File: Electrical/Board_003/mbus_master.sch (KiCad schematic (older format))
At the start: 14 parts, among them J1 Conn_01x02, J2 Conn_01x02, J3 Conn_01x02, Q1 BC337, Q2 BC337, Q3 BC337, Q4 BD136

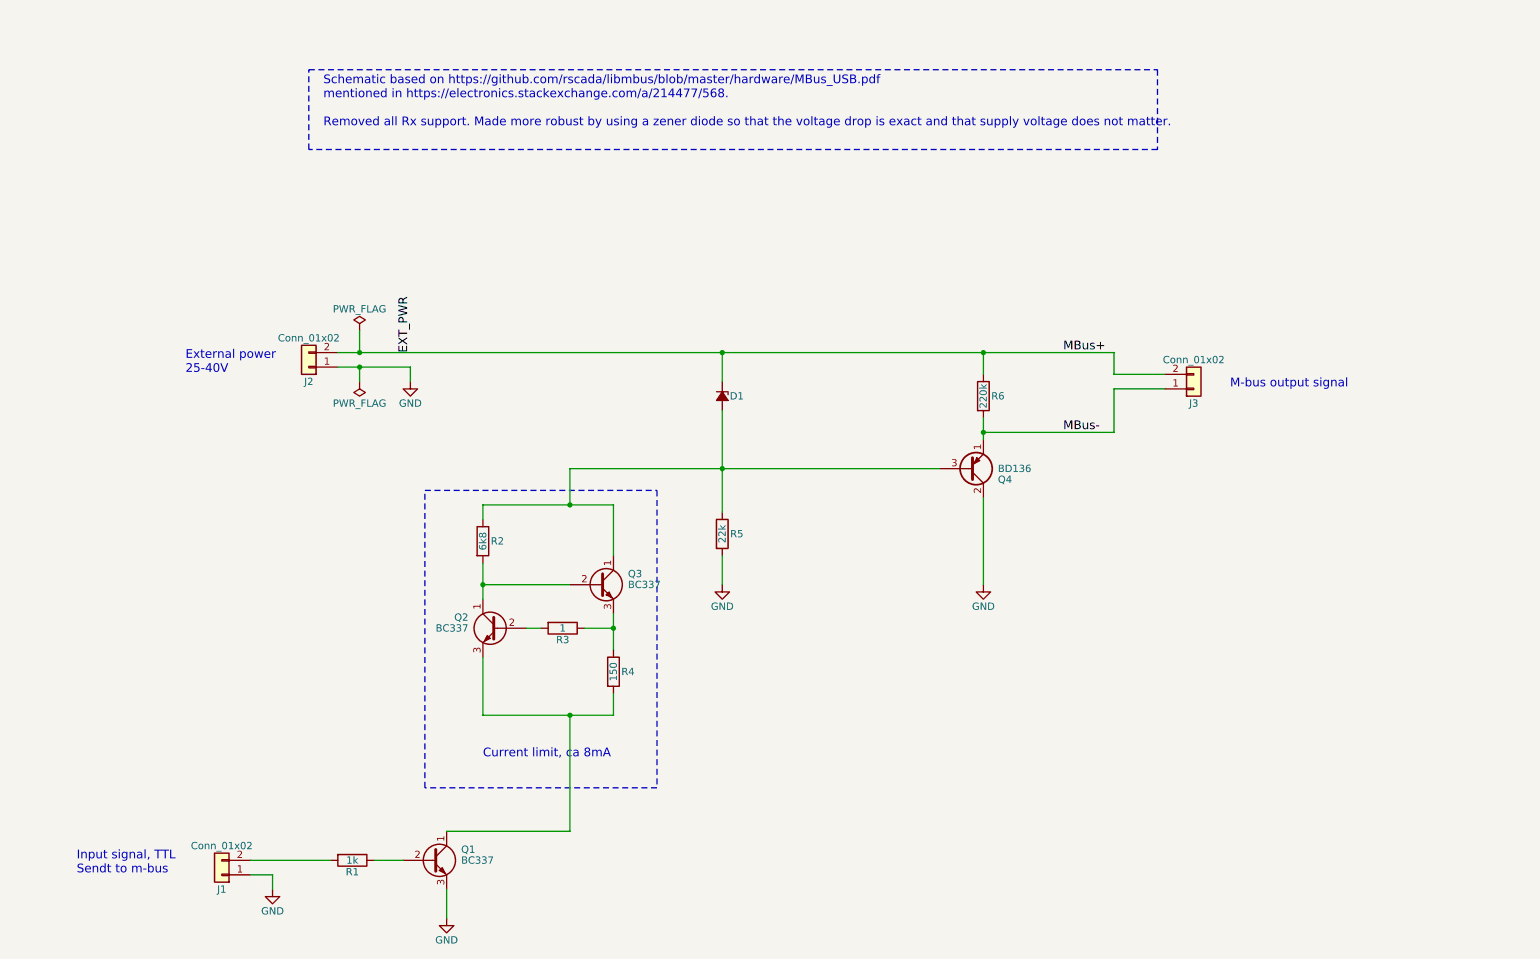
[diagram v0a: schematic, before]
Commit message: Update schematic to match mbus_master_100
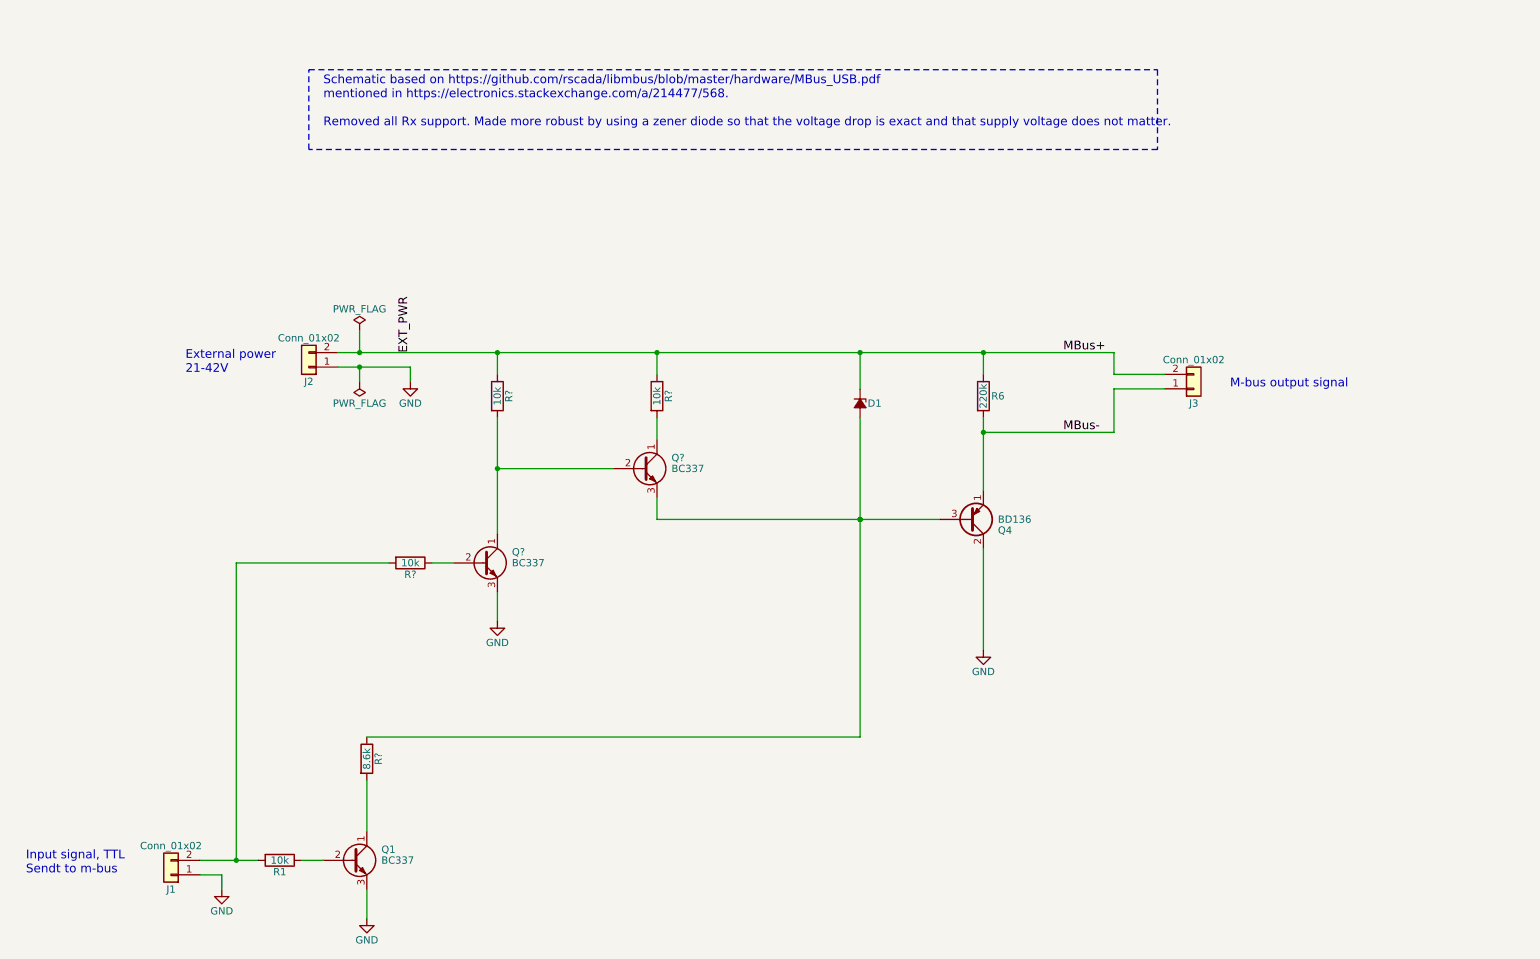
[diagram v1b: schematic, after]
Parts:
- removed Q2, Q3: BC337, TO_SOT_Packages_THT:TO-92_Molded_Narrow, symbol BC337
- removed R2: 6k8, Resistors_THT:R_Axial_DIN0207_L6.3mm_D2.5mm_P10.16mm_Horizontal, symbol R
- removed R3: 1, Resistors_THT:R_Axial_DIN0207_L6.3mm_D2.5mm_P10.16mm_Horizontal, symbol R
- removed R4: 150, Resistors_THT:R_Axial_DIN0207_L6.3mm_D2.5mm_P10.16mm_Horizontal, symbol R
- removed R5: 22k, Resistors_THT:R_Axial_DIN0207_L6.3mm_D2.5mm_P10.16mm_Horizontal, symbol R
- added Q? (x2): BC337, TO_SOT_Packages_THT:TO-92_Molded_Narrow, symbol BC337
- added R?: 8.6k, symbol R
- added R? (x3): 10k, symbol R
- R1: value 1k -> 10k
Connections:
- net EXT_PWR: now also R?.1, R?.1
- net GND: now also Q?.3 (E)
- net at J1.2 (Pin_2), R1.2: now also R?.2
- net at Q1.1 (C): now also R?.2
- net at D1.2 (A), Q4.3 (B): now also Q?.3 (E), R?.1
- new net: Q?.1 (C), Q?.2 (B), R?.2
- new net: Q?.2 (B), R?.1
- new net: Q?.1 (C), R?.2
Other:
- note added: "External power\n21-42V"
- note removed: "Current limit, ca 8mA"
- note removed: "External power\n25-40V"
- moved on the sheet: D1, J1, Q1, Q4, R1

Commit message: Update schematic and pcb to match mbus_master_101
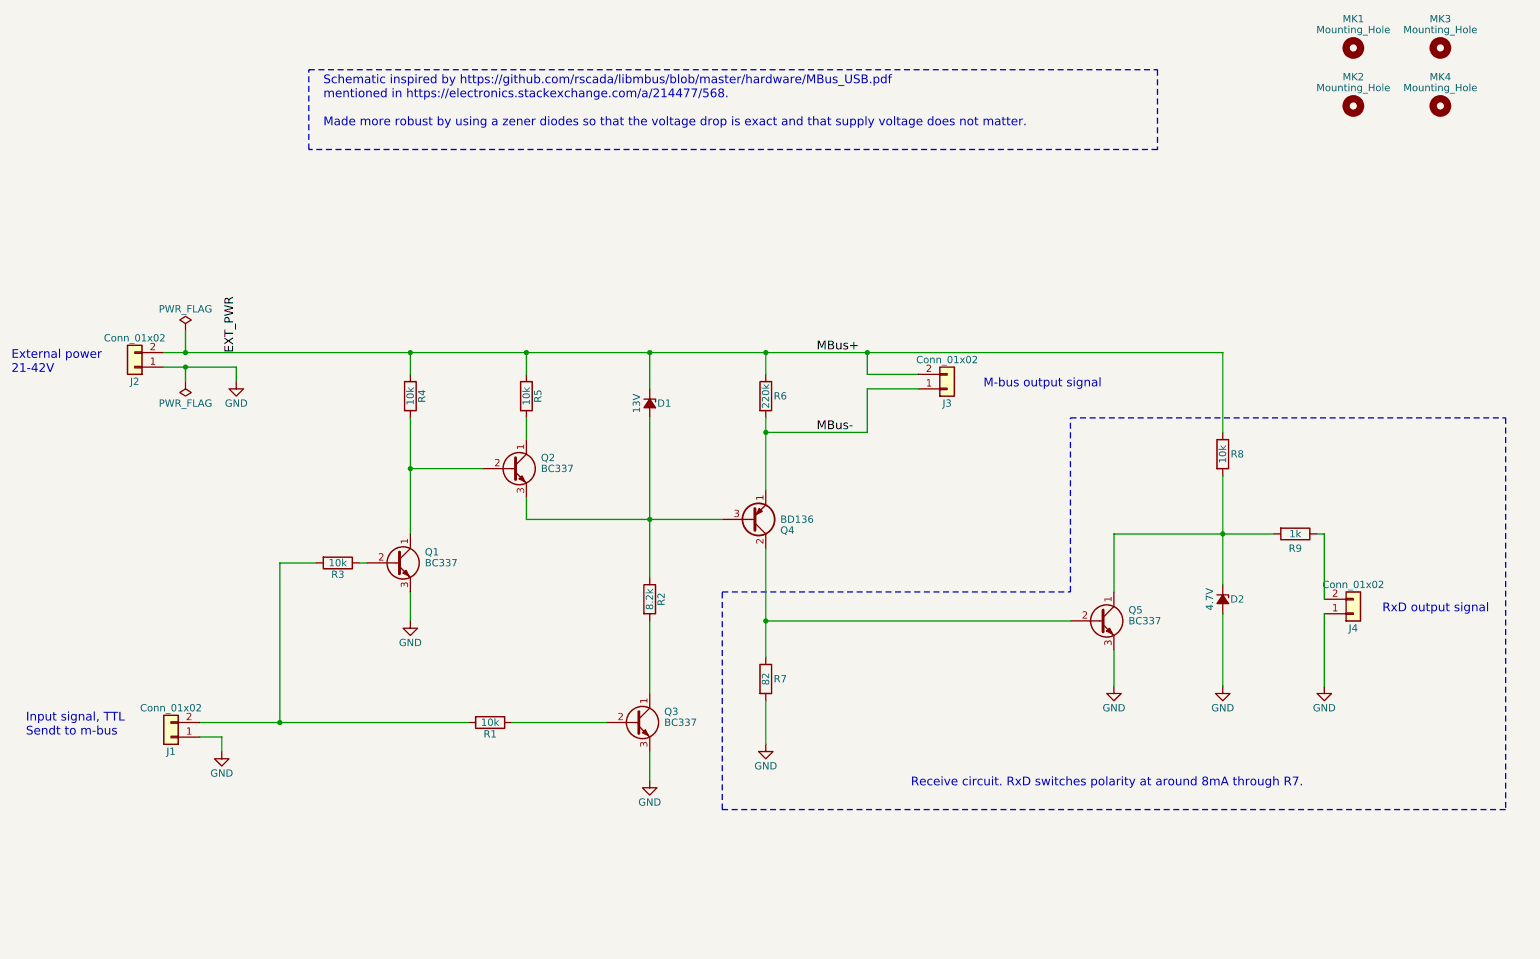
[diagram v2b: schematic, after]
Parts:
- added D2: 4.7V, Diodes_THT:D_A-405_P7.62mm_Horizontal, symbol D_Zener_Small_ALT
- added J4: Conn_01x02, Pin_Headers:Pin_Header_Straight_1x02_Pitch2.54mm, symbol Conn_01x02
- added MK1, MK2, MK3, MK4: Mounting_Hole, Mounting_Holes:MountingHole_4.3mm_M4_ISO14580, symbol Mounting_Hole
- added Q5: BC337, TO_SOT_Packages_THT:TO-92_Molded_Narrow, symbol BC337
- added R7: 82, Resistors_THT:R_Axial_DIN0207_L6.3mm_D2.5mm_P10.16mm_Horizontal, symbol R
- added R8: 10k, Resistors_THT:R_Axial_DIN0207_L6.3mm_D2.5mm_P10.16mm_Horizontal, symbol R
- added R9: 1k, Resistors_THT:R_Axial_DIN0207_L6.3mm_D2.5mm_P10.16mm_Horizontal, symbol R
- D1: value D_Zener_Small_ALT -> 13V; footprint Diodes_THT:D_A-405_P7.62mm_Horizontal -> Diodes_THT:D_5W_P12.70mm_Horizontal
- J1, J2, J3: footprint Pin_Headers:Pin_Header_Straight_1x02_Pitch1.27mm -> Pin_Headers:Pin_Header_Straight_1x02_Pitch2.54mm
- R2: renamed from R?; value 8.6k -> 8.2k; footprint (none) -> Resistors_THT:R_Axial_DIN0207_L6.3mm_D2.5mm_P10.16mm_Horizontal
- R3, R4, R5: renamed from R?; footprint (none) -> Resistors_THT:R_Axial_DIN0207_L6.3mm_D2.5mm_P10.16mm_Horizontal
- gave numbers to parts that had none: 2
- renumbered Q1 to Q3
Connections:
- net EXT_PWR: now also R8.1
- net GND: now also D2.2 (A), J4.1 (Pin_1), Q5.3 (E), R7.2; no longer Q4.2 (C)
- new net: Q4.2 (C), Q5.2 (B), R7.1
- new net: D2.1 (K), Q5.1 (C), R8.2, R9.2
- new net: J4.2 (Pin_2), R9.1
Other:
- note added: "Receive circuit. RxD switches polarity at around 8mA through R7."
- note added: "RxD output signal"
- note added: "Schematic inspired by https://github.com/rscada/libmbus/blob/master/hardware/MBus_USB.pdf\nmentioned in https://electronics.stackexchange.com/a/214477/568.\n\nMade more robust by using a zener diodes so that the voltage drop is exact and that supply voltage does not matter."
- note removed: "Schematic based on https://github.com/rscada/libmbus/blob/master/hardware/MBus_USB.pdf\nmentioned in https://electronics.stackexchange.com/a/214477/568.\n\nRemoved all Rx support. Made more robust by using a zener diode so that the voltage drop is exact and that supply voltage does not matter."
- moved on the sheet: D1, J1, J2, J3, Q1, Q2, Q3, Q4, R1, R2, R3, R4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
